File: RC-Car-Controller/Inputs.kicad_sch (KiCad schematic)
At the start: 6 parts, among them SW2 SW_Omron_B3FS, SW3 SW_Omron_B3FS

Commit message: Did some stuff on the Controller
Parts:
- removed R2: PTA6043-2015CPB103, symbol PTA6043-2015CPB103:PTA6043-2015CPB103
- removed R4, R5: 10k, Resistor_SMD:R_0201_0603Metric, symbol Device:R
- removed SW2, SW3: SW_Omron_B3FS, symbol Switch:SW_Omron_B3FS
- added R16, R2: 10k, Resistor_THT:R_Axial_DIN0309_L9.0mm_D3.2mm_P15.24mm_Horizontal, symbol Device:R
- added R17: PTA6043-2015CPB103, Potentiometer_THT:Potentiometer_Bourns_PTA6043_Single_Slide, symbol PTA6043-2015CPB103:PTA6043-2015CPB103
- added SW2, SW4: 1825027-8, SW2_1825027-C_TEC:SW2_1825027-C_TEC, symbol SW2_1825027-C_TEC:1825027-8
- R3: footprint (none) -> Potentiometer_THT:Potentiometer_Bourns_PTA6043_Single_Slide
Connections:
- net +3V3: now also R16.2, R17.1, R2.2
- net Button_L: now also R16.1, SW4.2
- net Button_R: now also R2.1, SW2.2
- net GND_3V3: now also R17.3, SW2.1, SW2.3, SW2.4, SW4.1, SW4.3, SW4.4
- net Slider_L: now also R17.2

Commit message: Did a bunch of stuff on the controller
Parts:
- R16, R2: footprint Resistor_THT:R_Axial_DIN0309_L9.0mm_D3.2mm_P15.24mm_Horizontal -> Capacitor_SMD:C_0603_1608Metric
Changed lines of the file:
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@@
 			)
 		)
-		(property "Footprint" "Resistor_THT:R_Axial_DIN0309_L9.0mm_D3.2mm_P15.24mm_Horizontal"
+		(property "Footprint" "Capacitor_SMD:C_0603_1608Metric"
 			(at 132.588 110.49 90)
 			(effects
@@
 			)
 		)
-		(property "Footprint" "Resistor_THT:R_Axial_DIN0309_L9.0mm_D3.2mm_P15.24mm_Horizontal"
+		(property "Footprint" "Capacitor_SMD:C_0603_1608Metric"
 			(at 170.688 110.49 90)
 			(effects

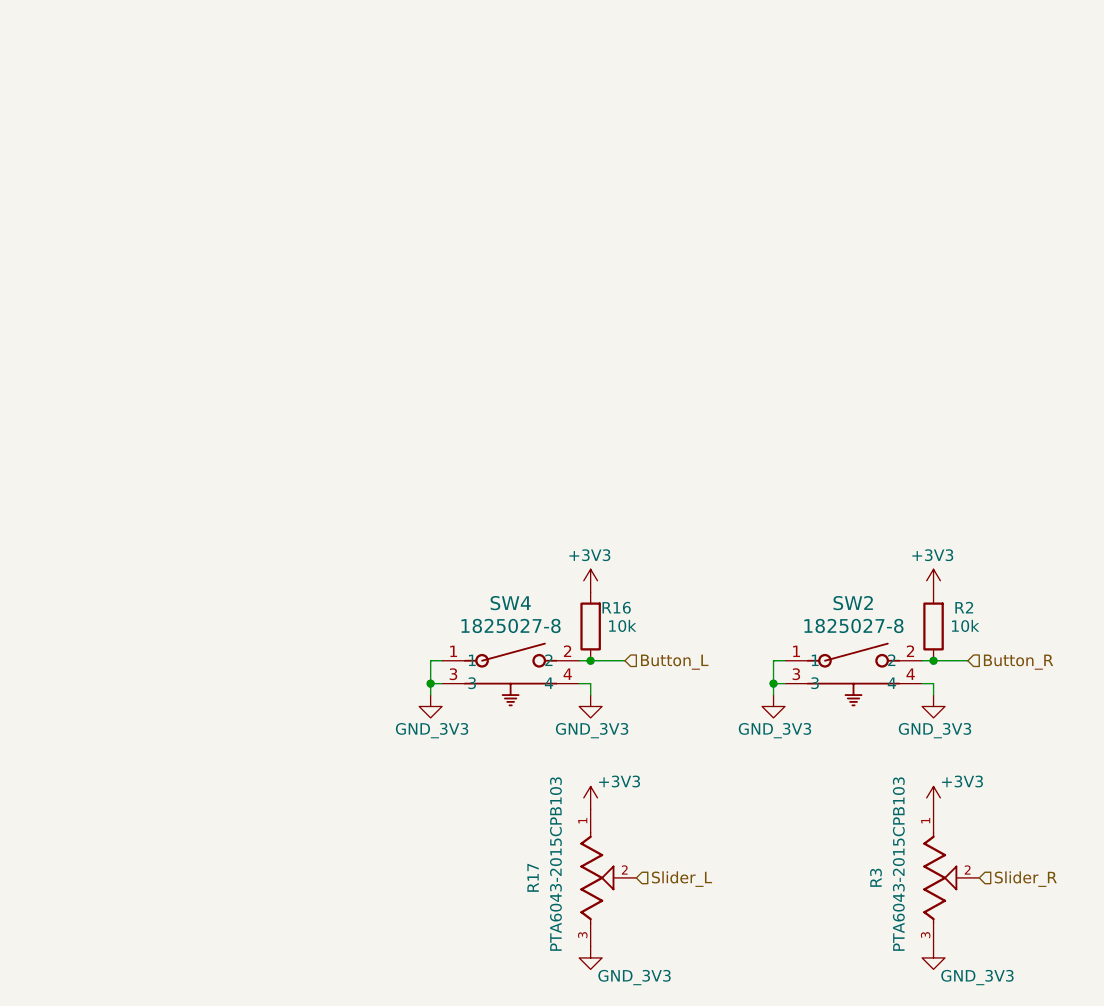
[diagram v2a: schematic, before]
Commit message: Finished non-RF Controller PCB
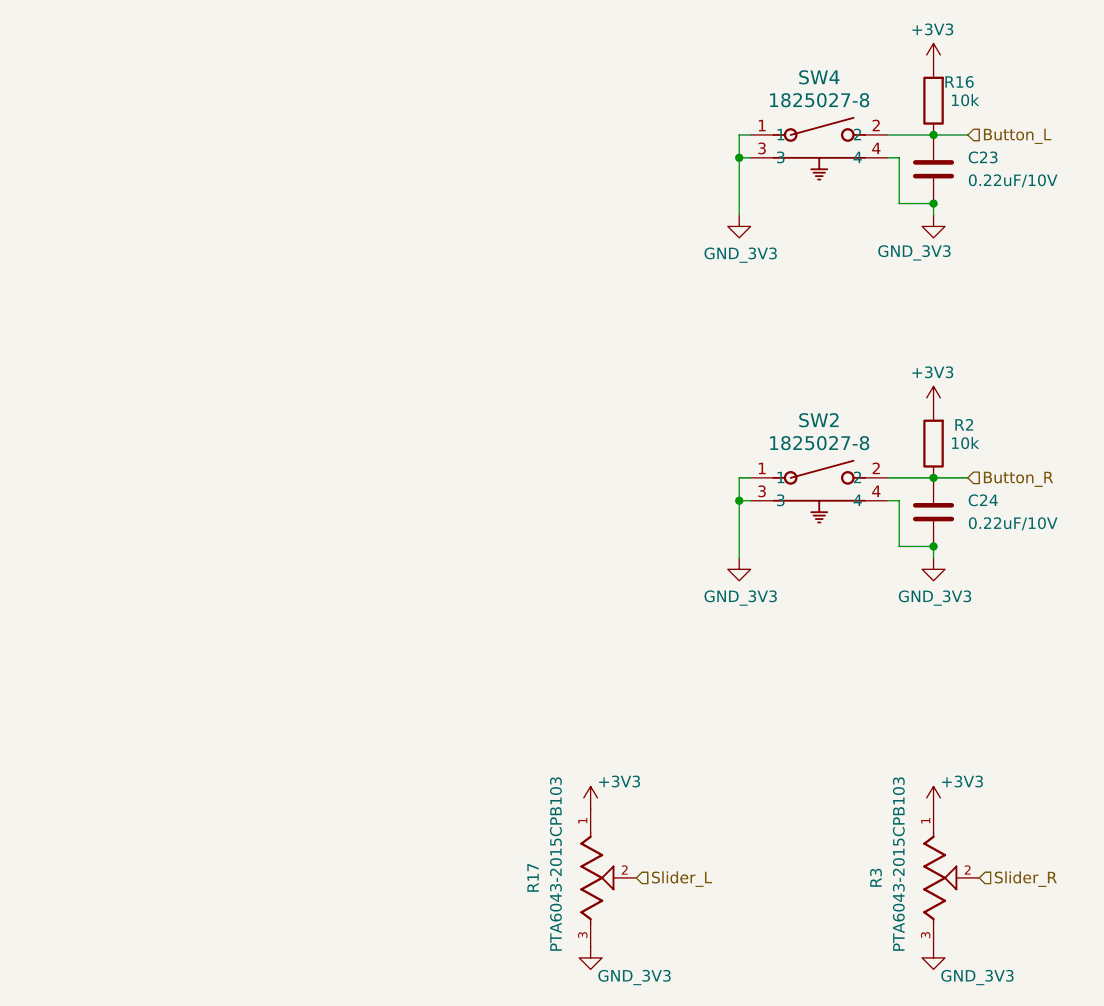
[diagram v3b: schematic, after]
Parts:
- added C23, C24: 0.22uF/10V, Capacitor_SMD:C_0603_1608Metric, symbol Device:C
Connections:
- net Button_L: now also C23.1
- net Button_R: now also C24.1
- net GND_3V3: now also C23.2, C24.2
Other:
- moved on the sheet: R16, R2, SW2, SW4

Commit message: Finished Controller PCB Pre-Review
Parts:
- renumbered C23 to C30, C24 to C31, R17 to R45, R16 to R46, R2 to R47, R3 to R48, SW4 to SW3, SW2 to SW4
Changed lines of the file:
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@@
 		(on_board yes)
 		(dnp no)
-		(property "Reference" "#PWR011"
+		(property "Reference" "#PWR093"
 			(at 168.91 134.62 0)
 			(effects
@@
 			(project "RC-Car-Controller"
 				(path "/ba870fd1-751d-4755-8e1a-1ea86ca9e2f6/2b1fa8b9-c985-4895-a194-2800399bdd10"
-					(reference "#PWR011")
+					(reference "#PWR093")
 					(unit 1)
 				)
@@
 		(on_board yes)
 		(dnp no)
-		(property "Reference" "#PWR012"
+		(property "Reference" "#PWR094"
 			(at 168.91 152.4 0)
 			(effects
@@
 			(project "RC-Car-Controller"
 				(path "/ba870fd1-751d-4755-8e1a-1ea86ca9e2f6/2b1fa8b9-c985-4895-a194-2800399bdd10"
-					(reference "#PWR012")
+					(reference "#PWR094")
 					(unit 1)
 				)
@@
 		(on_board yes)
 		(dnp no)
-		(property "Reference" "R3"
+		(property "Reference" "R48"
 			(at 162.56 138.43 0)
 			(effects
@@
 			(project "RC-Car-Controller"
 				(path "/ba870fd1-751d-4755-8e1a-1ea86ca9e2f6/2b1fa8b9-c985-4895-a194-2800399bdd10"
-					(reference "R3")
+					(reference "R48")
 					(unit 1)
 				)
@@
 		(on_board yes)
 		(dnp no)
-		(property "Reference" "#PWR0100"
+		(property "Reference" "#PWR089"
 			(at 168.91 52.07 0)
 			(effects
@@
 			(project "RC-Car-Controller"
 				(path "/ba870fd1-751d-4755-8e1a-1ea86ca9e2f6/2b1fa8b9-c985-4895-a194-2800399bdd10"
-					(reference "#PWR0100")
+					(reference "#PWR089")
 					(unit 1)
 				)
@@
 		(on_board yes)
 		(dnp no)
-		(property "Reference" "#PWR060"
+		(property "Reference" "#PWR092"
 			(at 168.91 109.22 0)
 			(effects
@@
 			(project "RC-Car-Controller"
 				(path "/ba870fd1-751d-4755-8e1a-1ea86ca9e2f6/2b1fa8b9-c985-4895-a194-2800399bdd10"
-					(reference "#PWR060")
+					(reference "#PWR092")
 					(unit 1)
 				)
@@
 		(dnp no)
 		(fields_autoplaced yes)
-		(property "Reference" "SW2"
+		(property "Reference" "SW4"
 			(at 156.21 87.63 0)
 			(effects
@@
 			(project "RC-Car-Controller"
 				(path "/ba870fd1-751d-4755-8e1a-1ea86ca9e2f6/2b1fa8b9-c985-4895-a194-2800399bdd10"
-					(reference "SW2")
+					(reference "SW4")
 					(unit 1)
 				)
@@
 		(on_board yes)
 		(dnp no)
-		(property "Reference" "#PWR0102"
+		(property "Reference" "#PWR085"
 			(at 130.81 134.62 0)
 			(effects
@@
 			(project "RC-Car-Controller"
 				(path "/ba870fd1-751d-4755-8e1a-1ea86ca9e2f6/2b1fa8b9-c985-4895-a194-2800399bdd10"
-					(reference "#PWR0102")
+					(reference "#PWR085")
 					(unit 1)
 				)
@@
 		(on_board yes)
 		(dnp no)
-		(property "Reference" "#PWR035"
+		(property "Reference" "#PWR088"
 			(at 147.32 109.22 0)
 			(effects
@@
 			(project "RC-Car-Controller"
 				(path "/ba870fd1-751d-4755-8e1a-1ea86ca9e2f6/2b1fa8b9-c985-4895-a194-2800399bdd10"
-					(reference "#PWR035")
+					(reference "#PWR088")
 					(unit 1)
 				)
@@
 		(on_board yes)
 		(dnp no)
-		(property "Reference" "#PWR0103"
+		(property "Reference" "#PWR086"
 			(at 130.81 152.4 0)
 			(effects
@@
 			(project "RC-Car-Controller"
 				(path "/ba870fd1-751d-4755-8e1a-1ea86ca9e2f6/2b1fa8b9-c985-4895-a194-2800399bdd10"
-					(reference "#PWR0103")
+					(reference "#PWR086")
 					(unit 1)
 				)
@@
 		(on_board yes)
 		(dnp no)
-		(property "Reference" "R17"
+		(property "Reference" "R45"
 			(at 124.46 138.43 0)
 			(effects
@@
 			(project "RC-Car-Controller"
 				(path "/ba870fd1-751d-4755-8e1a-1ea86ca9e2f6/2b1fa8b9-c985-4895-a194-2800399bdd10"
-					(reference "R17")
+					(reference "R45")
 					(unit 1)
 				)
@@
 		(dnp no)
 		(fields_autoplaced yes)
-		(property "Reference" "C24"
+		(property "Reference" "C31"
 			(at 172.72 96.5199 0)
 			(effects
@@
 			(project "RC-Car-Controller"
 				(path "/ba870fd1-751d-4755-8e1a-1ea86ca9e2f6/2b1fa8b9-c985-4895-a194-2800399bdd10"
-					(reference "C24")
+					(reference "C31")
 					(unit 1)
 				)
@@
 		(dnp no)
 		(fields_autoplaced yes)
-		(property "Reference" "C23"
+		(property "Reference" "C30"
 			(at 172.72 58.4199 0)
 			(effects
@@
 			(project "RC-Car-Controller"
 				(path "/ba870fd1-751d-4755-8e1a-1ea86ca9e2f6/2b1fa8b9-c985-4895-a194-2800399bdd10"
-					(reference "C23")
+					(reference "C30")
 					(unit 1)
 				)
@@
 		(on_board yes)
 		(dnp no)
-		(property "Reference" "R16"
+		(property "Reference" "R46"
 			(at 173.482 50.038 0)
 			(effects
@@
 			(project "RC-Car-Controller"
 				(path "/ba870fd1-751d-4755-8e1a-1ea86ca9e2f6/2b1fa8b9-c985-4895-a194-2800399bdd10"
-					(reference "R16")
+					(reference "R46")
 					(unit 1)
 				)
@@
 		(on_board yes)
 		(dnp no)
-		(property "Reference" "#PWR061"
+		(property "Reference" "#PWR087"
 			(at 147.32 71.12 0)
 			(effects
@@
 			(project "RC-Car-Controller"
 				(path "/ba870fd1-751d-4755-8e1a-1ea86ca9e2f6/2b1fa8b9-c985-4895-a194-2800399bdd10"
-					(reference "#PWR061")
+					(reference "#PWR087")
 					(unit 1)
 				)
@@
 		(dnp no)
 		(fields_autoplaced yes)
-		(property "Reference" "SW4"
+		(property "Reference" "SW3"
 			(at 156.21 49.53 0)
 			(effects
@@
 			(project "RC-Car-Controller"
 				(path "/ba870fd1-751d-4755-8e1a-1ea86ca9e2f6/2b1fa8b9-c985-4895-a194-2800399bdd10"
-					(reference "SW4")
+					(reference "SW3")
 					(unit 1)
 				)
@@
 		(on_board yes)
 		(dnp no)
-		(property "Reference" "#PWR06"
+		(property "Reference" "#PWR091"
 			(at 168.91 90.17 0)
 			(effects
@@
 			(project "RC-Car-Controller"
 				(path "/ba870fd1-751d-4755-8e1a-1ea86ca9e2f6/2b1fa8b9-c985-4895-a194-2800399bdd10"
-					(reference "#PWR06")
+					(reference "#PWR091")
 					(unit 1)
 				)
@@
 		(on_board yes)
 		(dnp no)
-		(property "Reference" "R2"
+		(property "Reference" "R47"
 			(at 173.482 88.138 0)
 			(effects
@@
 			(project "RC-Car-Controller"
 				(path "/ba870fd1-751d-4755-8e1a-1ea86ca9e2f6/2b1fa8b9-c985-4895-a194-2800399bdd10"
-					(reference "R2")
+					(reference "R47")
 					(unit 1)
 				)
@@
 		(on_board yes)
 		(dnp no)
-		(property "Reference" "#PWR059"
+		(property "Reference" "#PWR090"
 			(at 168.91 71.12 0)
 			(effects
@@
 			(project "RC-Car-Controller"
 				(path "/ba870fd1-751d-4755-8e1a-1ea86ca9e2f6/2b1fa8b9-c985-4895-a194-2800399bdd10"
-					(reference "#PWR059")
-					(unit 1)
-				)
+					(reference "#PWR090")
+					(unit 1)
+				)

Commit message: most resistors given PNs
most resistors given PNs. some remaining
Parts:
- R46, R47: MANUF_PN (none) -> RC0603FR-0710KL
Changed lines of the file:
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@@
+			)
+		)
+		(property "MANUF_PN" ""
+			(at 168.91 138.43 0)
+			(effects
+				(font
+					(size 1.27 1.27)
+				)
+				(hide yes)
 			)
 		)
@@
 			)
 		)
+		(property "MANUF_PN" ""
+			(at 148.59 93.98 0)
+			(effects
+				(font
+					(size 1.27 1.27)
+				)
+				(hide yes)
+			)
+		)
 		(pin "1"
 		)
@@
 				)
 				(justify bottom)
+				(hide yes)
+			)
+		)
+		(property "MANUF_PN" ""
+			(at 130.81 138.43 0)
+			(effects
+				(font
+					(size 1.27 1.27)
+				)
 				(hide yes)
 			)
@@
 			)
 		)
+		(property "MANUF_PN" ""
+			(at 168.91 97.79 0)
+			(effects
+				(font
+					(size 1.27 1.27)
+				)
+				(hide yes)
+			)
+		)
 		(pin "1"
 		)
@@
 			)
 		)
+		(property "MANUF_PN" ""
+			(at 168.91 59.69 0)
+			(effects
+				(font
+					(size 1.27 1.27)
+				)
+				(hide yes)
+			)
+		)
 		(pin "1"
 		)
@@
 		)
 		(property "Description" "Resistor"
+			(at 168.91 52.07 0)
+			(effects
+				(font
+					(size 1.27 1.27)
+				)
+				(hide yes)
+			)
+		)
+		(property "MANUF_PN" "RC0603FR-0710KL"
 			(at 168.91 52.07 0)
 			(effects
@@
 			)
 		)
+		(property "MANUF_PN" ""
+			(at 148.59 55.88 0)
+			(effects
+				(font
+					(size 1.27 1.27)
+				)
+				(hide yes)
+			)
+		)
 		(pin "1"
 		)
@@
 			(at 168.91 90.17 0)
 			(effects
+				(font
+					(size 1.27 1.27)
+				)
+				(hide yes)
+			)
+		)
+		(property "MANUF_PN" "RC0603FR-0710KL"
+			(at 168.91 90.17 0)
+			(effects

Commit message: controller cpnts given MANUF_PNs
controller cpnts given MANUF_PNs. not all components, but all resistors are done
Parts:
- R45, R48: MANUF_PN (none) -> PTA6043-2015CPB103
- SW3, SW4: MANUF_PN (none) -> 1825027-8
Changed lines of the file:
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@@
 			)
 		)
-		(property "MANUF_PN" ""
+		(property "MANUF_PN" "PTA6043-2015CPB103"
 			(at 168.91 138.43 0)
 			(effects
@@
 			)
 		)
-		(property "MANUF_PN" ""
+		(property "MANUF_PN" "1825027-8"
 			(at 148.59 93.98 0)
 			(effects
@@
 			)
 		)
-		(property "MANUF_PN" ""
+		(property "MANUF_PN" "PTA6043-2015CPB103"
 			(at 130.81 138.43 0)
 			(effects
@@
 			)
 		)
-		(property "MANUF_PN" ""
+		(property "MANUF_PN" "1825027-8"
 			(at 148.59 55.88 0)
 			(effects

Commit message: Filled out some Controller Caps
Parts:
- C30, C31: value 0.22uF/10V -> 0.1uF/10V; MANUF_PN (none) -> C0603C104K5RAC7411
- R46, R47: value 10k -> 10kohm
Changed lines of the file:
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@@
 			)
 		)
-		(property "Value" "0.22uF/10V"
+		(property "Value" "0.1uF/10V"
 			(at 172.72 99.0599 0)
 			(effects
@@
 			)
 		)
-		(property "MANUF_PN" ""
+		(property "MANUF_PN" "C0603C104K5RAC7411"
 			(at 168.91 97.79 0)
 			(effects
@@
 			)
 		)
-		(property "Value" "0.22uF/10V"
+		(property "Value" "0.1uF/10V"
 			(at 172.72 60.9599 0)
 			(effects
@@
 			)
 		)
-		(property "MANUF_PN" ""
+		(property "MANUF_PN" "C0603C104K5RAC7411"
 			(at 168.91 59.69 0)
 			(effects
@@
 			)
 		)
-		(property "Value" "10k"
-			(at 173.99 52.07 0)
+		(property "Value" "10kohm"
+			(at 177.8 52.324 0)
 			(effects
 				(font
@@
 			)
 		)
-		(property "Value" "10k"
-			(at 173.99 90.17 0)
-			(effects
-				(font
+		(property "Value" "10kohm"
+			(at 177.8 90.17 0)
+			(effects
+				(font
